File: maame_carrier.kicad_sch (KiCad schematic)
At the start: 64 parts, among them J1 To Kakute H7 V1.5: left strip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, J10 FS-iA10B iBUS servo lead (S +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, J11 TF-Luna pin order 1-6 (CFG ti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, J12 Spare FC I2C (5 V supply, sha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, J13 Payload servo power (+ -); se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, J17 Kakute spare: T3 RSSI 3V3(FC)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, J18 Pi SPI0, 3V3 logic, J20 VBAT OUT 6S fused (JST-XH 2-p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, J21 9V OUT from Kakute VTX 9V (JS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, J22 12V OUT 2A (JST-XH), J3 VBAT tap from ESC battery pad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, J6 Spare power: 5V_AUX G 5V_FC G, J7 Pi expansion: 3V3 logic ONLY, J8 TBS M10Q: order matches its p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, J9 SiK radio (UART4), U1 Raspberry Pi Zero W v1.1, com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, U2 TPS54360BDDAR 60V 3.5A buck, U3 TPS54360BDDAR 12V 2A buck

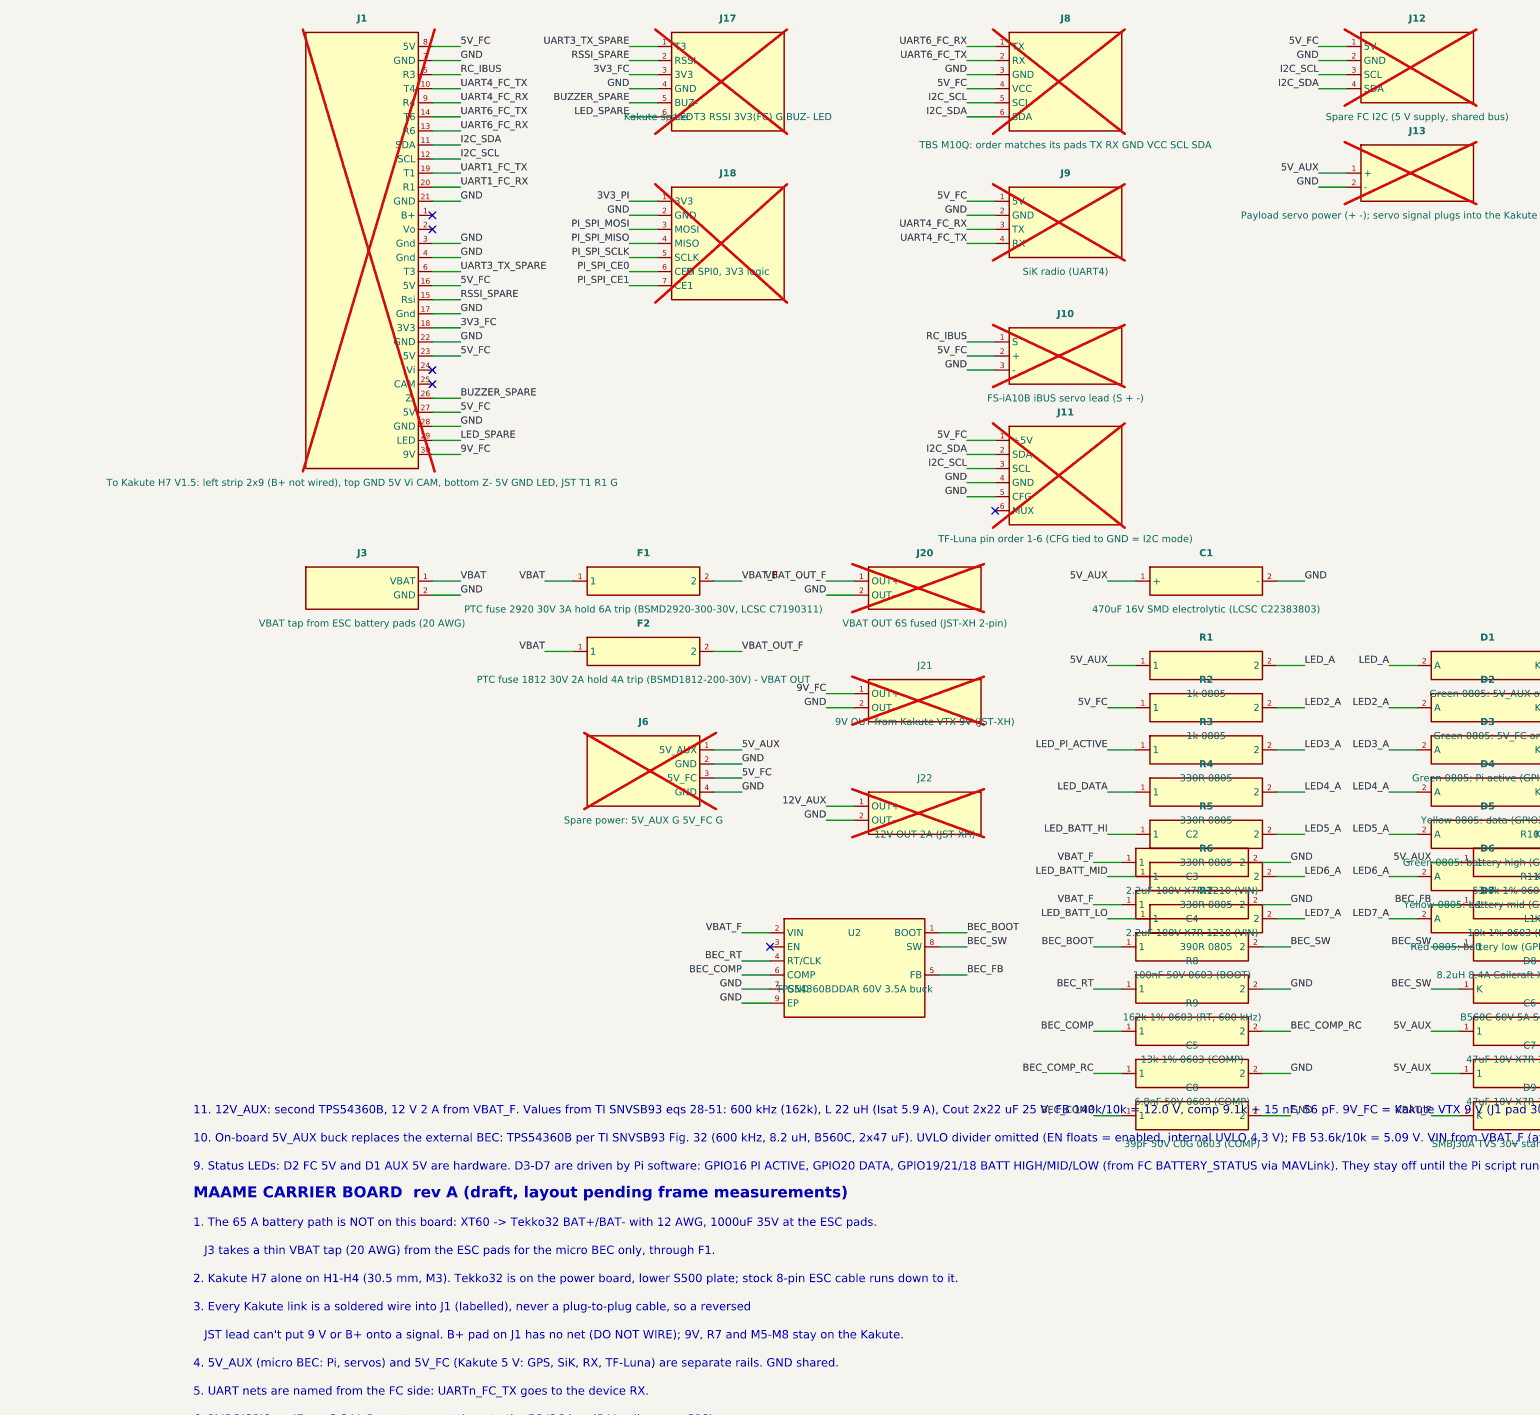
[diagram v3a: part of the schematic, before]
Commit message: Kakute connections as JLC-fitted 2.54 mm male headers (J1 2x9, J23/J24/J25 1x4) on the old pad positions; harness + assembly notes; re-routed, DRC 0 errors; fab regenerated incl. THT in CPL
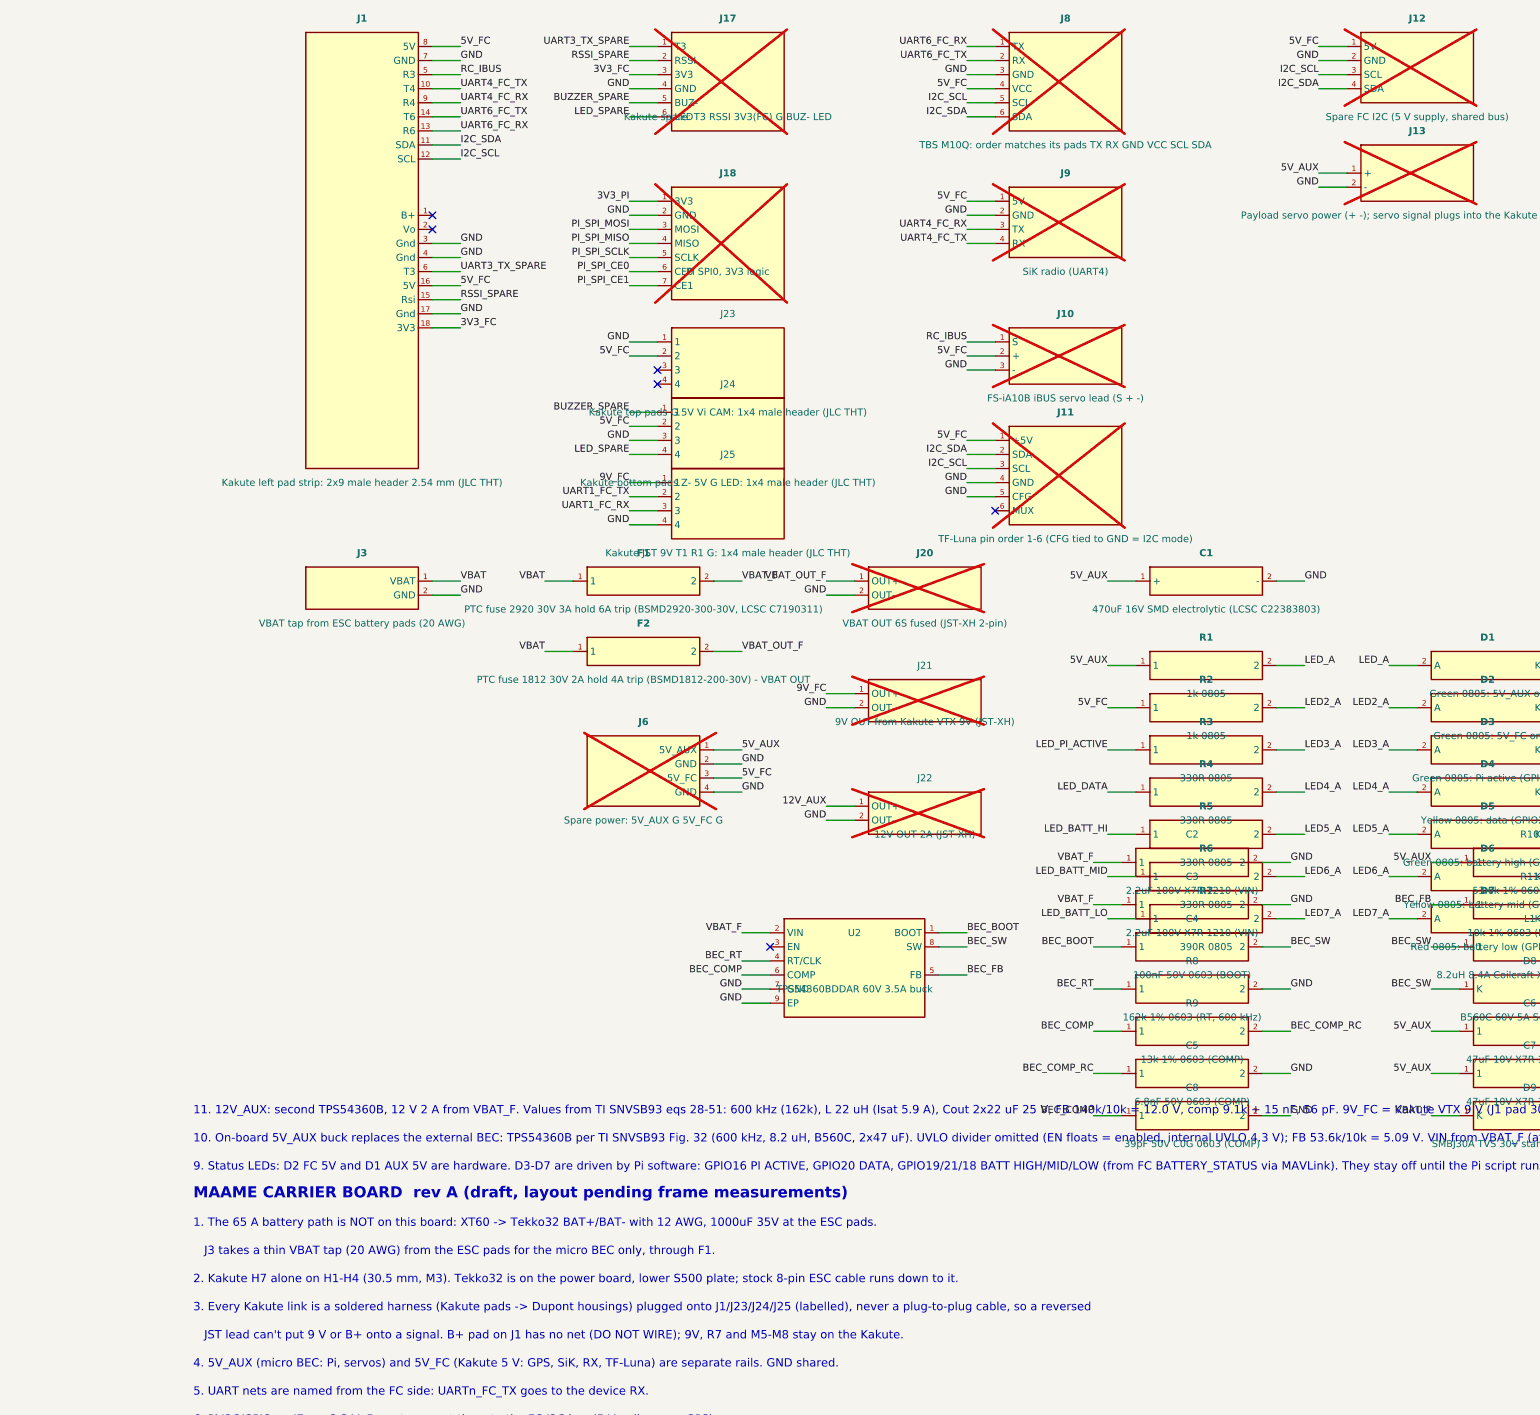
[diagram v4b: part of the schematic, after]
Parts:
- added J23: Kakute top pads G 5V Vi CAM: 1x4 male header (JLC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, Connector_PinHeader_2.54mm:PinHeader_1x04_P2.54mm_Vertical, symbol maame_carrier:HDR_1x4
- added J24: Kakute bottom pads Z- 5V G LED: 1x4 male header (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, Connector_PinHeader_2.54mm:PinHeader_1x04_P2.54mm_Vertical, symbol maame_carrier:HDR_1x4
- added J25: Kakute JST 9V T1 R1 G: 1x4 male header (JLC THT), Connector_PinHeader_2.54mm:PinHeader_1x04_P2.54mm_Vertical, symbol maame_carrier:HDR_1x4
- J1: value To Kakute H7 V1.5: left strip 2x9 (B+ not wired), top GND 5V Vi CAM, bottom Z- 5V GND LED, JST T1 R1 G -> Kakute left pad strip: 2x9 male header 2.54 mm (JLC THT); footprint maame_carrier:Kakute_Pads_2x9_R3 -> Connector_PinHeader_2.54mm:PinHeader_2x09_P2.54mm_Vertical; LCSC (none) -> C42372517; now fitted
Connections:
- net 5V_FC: now also J23.2, J24.2; no longer J1.23 (5V), J1.27 (5V)
- net 9V_FC: now also J25.1; no longer J1.30 (9V)
- net BUZZER_SPARE: now also J24.1; no longer J1.26 (Z-)
- net GND: now also J23.1, J24.3, J25.4; no longer J1.21 (GND), J1.22 (GND), J1.28 (GND)
- net LED_SPARE: now also J24.4; no longer J1.29 (LED)
- net UART1_FC_RX: now also J25.3; no longer J1.20 (R1)
- net UART1_FC_TX: now also J25.2; no longer J1.19 (T1)
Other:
- note added: "3. Every Kakute link is a soldered harness (Kakute pads -> Dupont housings) plugged onto J1/J23/J24/J25 (labelled), never a plug-to-plug cable, so a reversed"
- note removed: "3. Every Kakute link is a soldered wire into J1 (labelled), never a plug-to-plug cable, so a reversed"

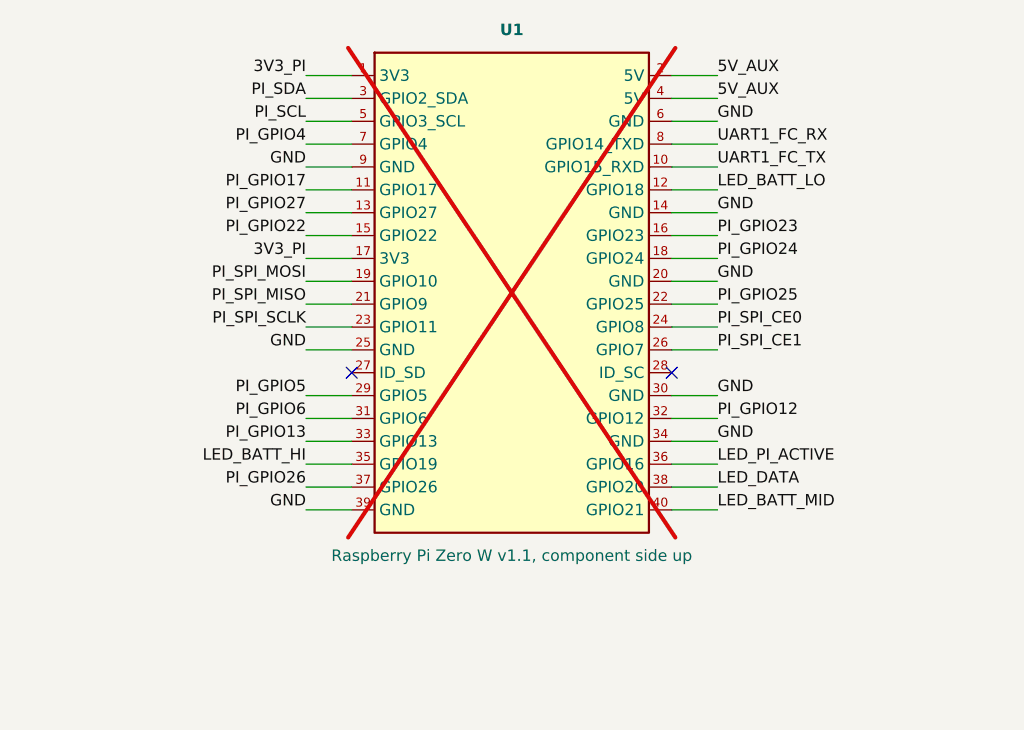
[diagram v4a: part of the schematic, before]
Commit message: Pi socket U1 (2x20 female 2.54 mm, 8.5 mm, C5124634) JLC-fitted; CPL uses pad centres for THT headers; assembly notes updated
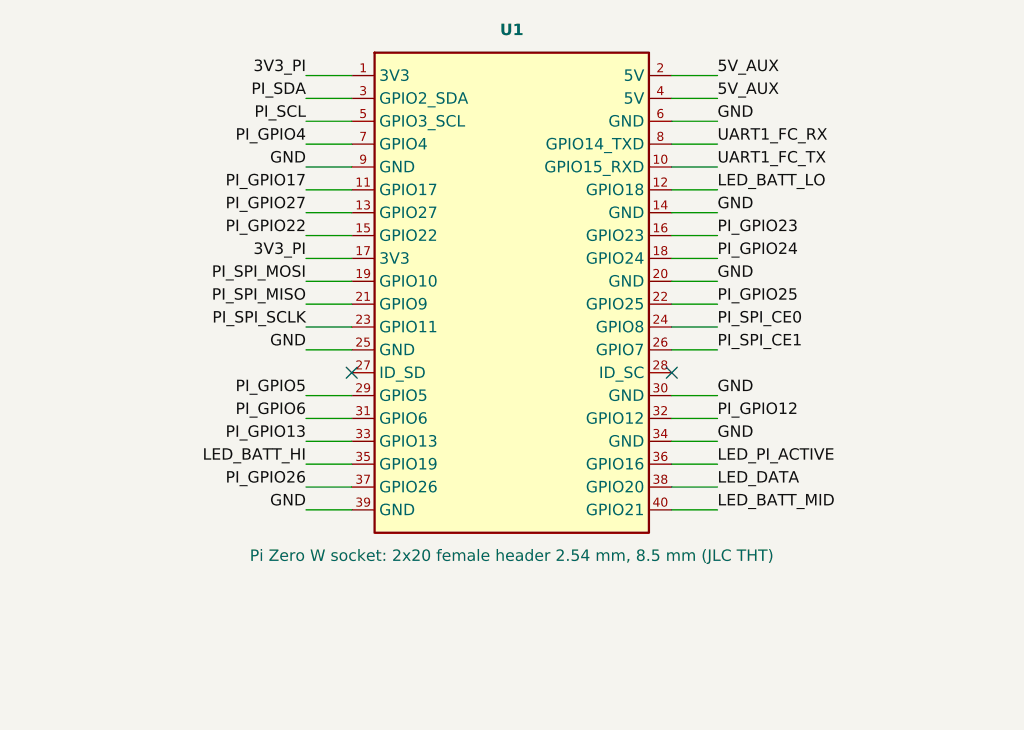
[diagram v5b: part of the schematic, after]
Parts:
- U1: value Raspberry Pi Zero W v1.1, component side up -> Pi Zero W socket: 2x20 female header 2.54 mm, 8.5 mm (JLC THT); LCSC (none) -> C5124634; now fitted
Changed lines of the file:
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@@
 		(on_board yes)
 		(in_pos_files yes)
-		(dnp yes)
+		(dnp no)
 		(property "Reference" "U1"
 			(at 330.2 30.48 0)
@@
 			)
 		)
-		(property "Value" "Raspberry Pi Zero W v1.1, component side up"
+		(property "Value" "Pi Zero W socket: 2x20 female header 2.54 mm, 8.5 mm (JLC THT)"
 			(at 330.2 88.9 0)
 			(show_name no)
@@
 			(show_name no)
 			(do_not_autoplace no)
+			(effects
+				(font
+					(size 1.27 1.27)
+				)
+			)
+		)
+		(property "LCSC" "C5124634"
+			(at 330.2 35.56 0)
+			(hide yes)
+			(show_name no)
+			(do_not_autoplace no)
